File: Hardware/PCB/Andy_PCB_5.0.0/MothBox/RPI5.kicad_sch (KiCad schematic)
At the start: 4 parts, among them U16 Female Inv Socket Pi 2.54-2*20, U18 RASPBERRY_PI_4B_4GB, U4 RASPBERRY_PI_4B_4GB, U5 RASPBERRY_PI_5

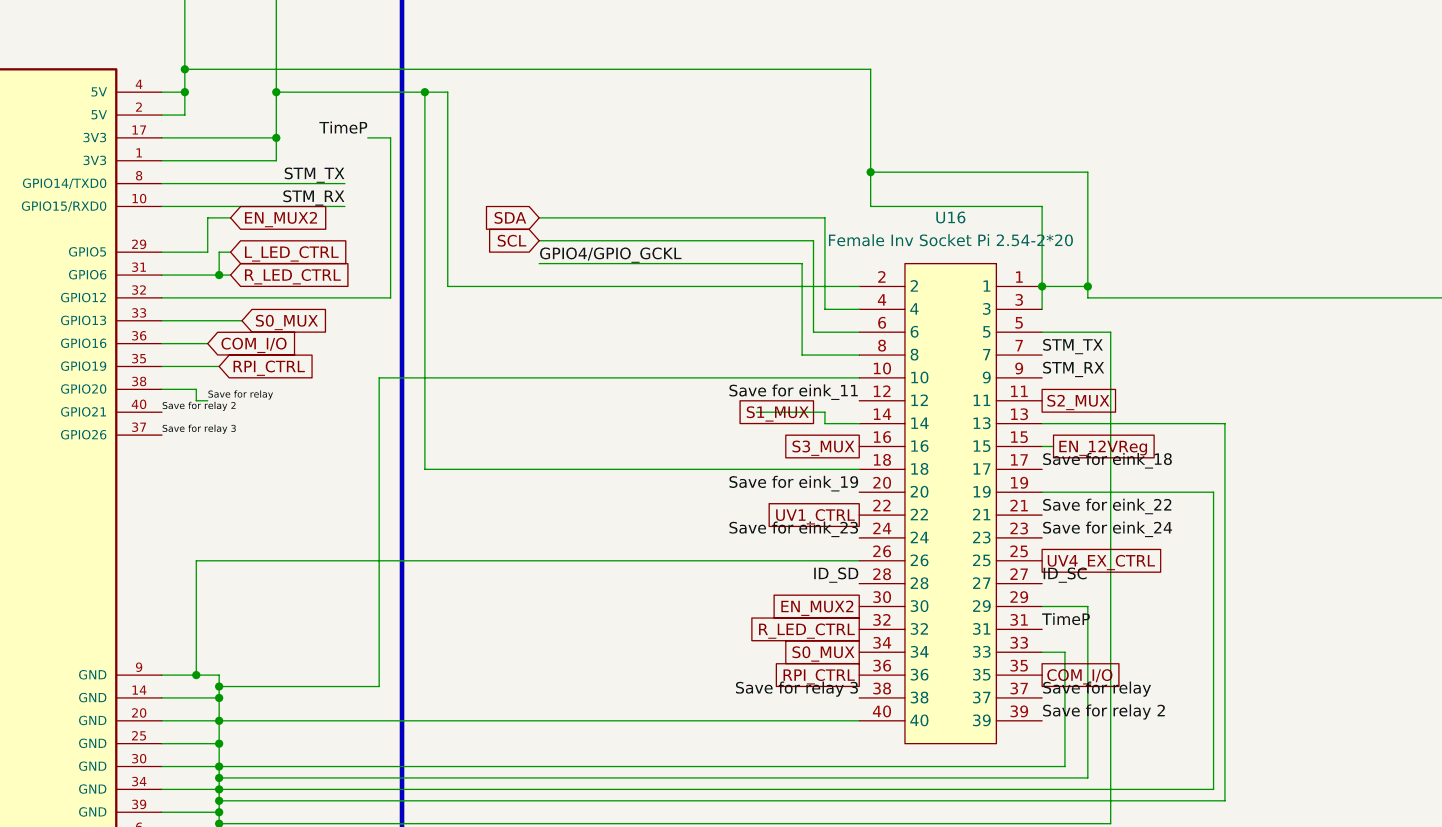
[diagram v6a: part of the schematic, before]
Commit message: added GPS 2 kinds
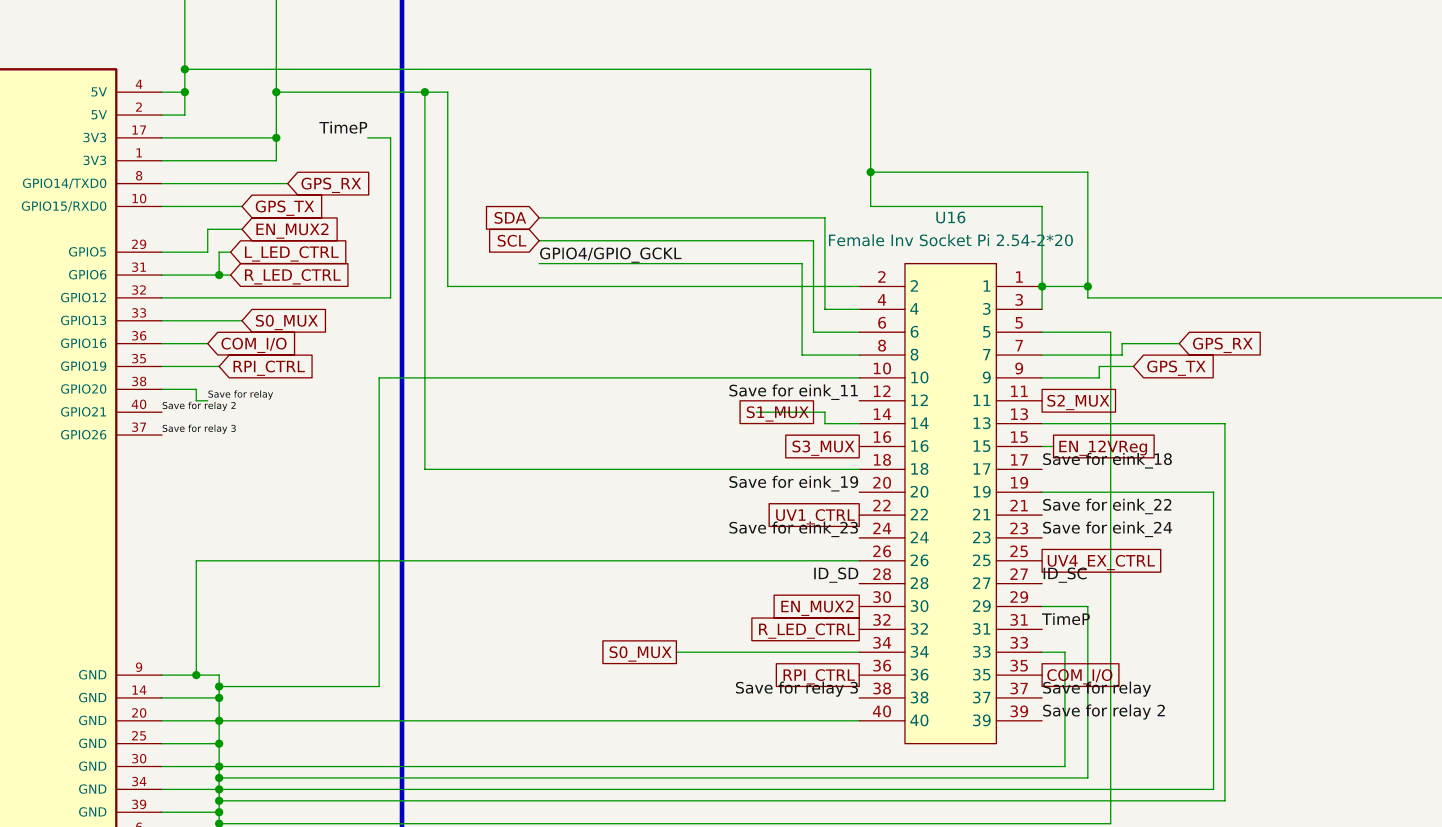
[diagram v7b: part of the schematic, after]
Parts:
- U5: footprint Connector_PinHeader_2.54mm:PinHeader_2x20_P2.54mm_Vertical -> AQLibrary:EPAPER_PinHeader_2x20_P2.54mm_Vertical
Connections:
- net STM_RX renamed GPS_TX
- net STM_TX renamed GPS_RX
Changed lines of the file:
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@@
+	(wire
+		(pts
+			(xy 153.67 102.87) (xy 173.99 102.87)
+		)
+		(stroke
+			(width 0)
+			(type default)
+		)
+	)
 	(wire
 		(pts
@@
 	(wire
 		(pts
-			(xy 96.52 53.34) (xy 116.84 53.34)
+			(xy 96.52 53.34) (xy 105.41 53.34)
 		)
 		(stroke
@@
 	(wire
 		(pts
+			(xy 200.66 72.39) (xy 200.66 71.12)
+		)
+		(stroke
+			(width 0)
+			(type default)
+		)
+	)
+	(wire
+		(pts
 			(xy 194.31 53.34) (xy 175.26 53.34)
 		)
@@
 	(wire
 		(pts
+			(xy 194.31 72.39) (xy 200.66 72.39)
+		)
+		(stroke
+			(width 0)
+			(type default)
+		)
+	)
+	(wire
+		(pts
 			(xy 102.87 110.49) (xy 173.99 110.49)
 		)
@@
 	(wire
 		(pts
-			(xy 101.6 54.61) (xy 104.14 54.61)
+			(xy 101.6 55.88) (xy 105.41 55.88)
 		)
 		(stroke
@@
 	(wire
 		(pts
-			(xy 96.52 50.8) (xy 116.84 50.8)
+			(xy 96.52 50.8) (xy 110.49 50.8)
 		)
 		(stroke
@@
 	(wire
 		(pts
+			(xy 203.2 69.85) (xy 203.2 68.58)
+		)
+		(stroke
+			(width 0)
+			(type default)
+		)
+	)
+	(wire
+		(pts
 			(xy 96.52 66.04) (xy 105.41 66.04)
 		)
@@
 	(wire
 		(pts
+			(xy 203.2 68.58) (xy 209.55 68.58)
+		)
+		(stroke
+			(width 0)
+			(type default)
+		)
+	)
+	(wire
+		(pts
 			(xy 173.99 72.39) (xy 120.65 72.39)
 		)
@@
 	(wire
 		(pts
+			(xy 194.31 69.85) (xy 203.2 69.85)
+		)
+		(stroke
+			(width 0)
+			(type default)
+		)
+	)
+	(wire
+		(pts
 			(xy 102.87 119.38) (xy 102.87 120.65)
 		)
@@
 	(wire
 		(pts
+			(xy 200.66 71.12) (xy 204.47 71.12)
+		)
+		(stroke
+			(width 0)
+			(type default)
+		)
+	)
+	(wire
+		(pts
 			(xy 170.18 64.77) (xy 170.18 54.61)
 		)
@@
 	(wire
 		(pts
-			(xy 101.6 54.61) (xy 101.6 58.42)
+			(xy 101.6 55.88) (xy 101.6 58.42)
 		)
 		(stroke
@@
 		)
 	)
-	(label "STM_TX"
-		(at 116.84 50.8 180)
-		(effects
-			(font
-				(size 1.27 1.27)
-			)
-			(justify right bottom)
-		)
-	)
 	(label "ID_SC"
 		(at 45.72 93.98 180)
@@
 		)
 	)
-	(label "STM_RX"
-		(at 194.31 72.39 0)
-		(effects
-			(font
-				(size 1.27 1.27)
-			)
-			(justify left bottom)
-		)
-	)
-	(label "STM_TX"
-		(at 194.31 69.85 0)
-		(effects
-			(font
-				(size 1.27 1.27)
-			)
-			(justify left bottom)
-		)
-	)
 	(label "Save for eink_23"
 		(at 45.72 81.28 180)
@@
 			(font
 				(size 0.762 0.762)
-			)
-			(justify right bottom)
-		)
-	)
-	(label "STM_RX"
-		(at 116.84 53.34 180)
-		(effects
-			(font
-				(size 1.27 1.27)
 			)
 			(justify right bottom)
@@
 	(global_label "S0_MUX"
 		(shape passive)
-		(at 173.99 102.87 180)
+		(at 153.67 102.87 180)
 		(effects
 			(font
@@
 		)
 		(property "Intersheetrefs" "${INTERSHEET_REFS}"
-			(at 173.99 102.87 0)
+			(at 153.67 102.87 0)
 			(effects
 				(font
@@
 		)
 	)
+	(global_label "GPS_RX"
+		(shape input)
+		(at 209.55 68.58 0)
+		(fields_autoplaced yes)
+		(effects
+			(font
+				(size 1.27 1.27)
+			)
+			(justify left)
+		)
+		(property "Intersheetrefs" "${INTERSHEET_REFS}"
+			(at 219.7318 68.58 0)
+			(effects
+				(font
+					(size 1.27 1.27)
+				)
+				(justify left)
+				(hide yes)
+			)
+		)
+	)
 	(global_label "SDA"
 		(shape input)
@@
 		)
 	)
+	(global_label "GPS_TX"
+		(shape input)
+		(at 204.47 71.12 0)
+		(fields_autoplaced yes)
+		(effects
+			(font
+				(size 1.27 1.27)
+			)
+			(justify left)
+		)
+		(property "Intersheetrefs" "${INTERSHEET_REFS}"
+			(at 214.3494 71.12 0)
+			(effects
+				(font
+					(size 1.27 1.27)
+				)
+				(justify left)
+				(hide yes)
+			)
+		)
+	)
 	(global_label "SCL"
 		(shape input)
@@
 		)
 	)
+	(global_label "GPS_RX"
+		(shape input)
+		(at 110.49 50.8 0)
+		(fields_autoplaced yes)
+		(effects
+			(font
+				(size 1.27 1.27)
+			)
+			(justify left)
+		)
+		(property "Intersheetrefs" "${INTERSHEET_REFS}"
+			(at 120.6718 50.8 0)
+			(effects
+				(font
+					(size 1.27 1.27)
+				)
+				(justify left)
+				(hide yes)
+			)
+		)
+	)
 	(global_label "R_LED_CTRL"
 		(shape passive)
@@
 	(global_label "EN_MUX2"
 		(shape input)
-		(at 104.14 54.61 0)
+		(at 105.41 55.88 0)
 		(fields_autoplaced yes)
 		(effects
@@
 		)
 		(property "Intersheetrefs" "${INTERSHEET_REFS}"
-			(at 115.7732 54.61 0)
+			(at 117.0432 55.88 0)
+			(effects
+				(font
+					(size 1.27 1.27)
+				)
+				(justify left)
+				(hide yes)
+			)
+		)
+	)
+	(global_label "GPS_TX"
+		(shape input)
+		(at 105.41 53.34 0)
+		(fields_autoplaced yes)
+		(effects
+			(font
+				(size 1.27 1.27)
+			)
+			(justify left)
+		)
+		(property "Intersheetrefs" "${INTERSHEET_REFS}"
+			(at 115.2894 53.34 0)
 			(effects
 				(font
@@
 			)
 		)
-		(property "Footprint" "Connector_PinHeader_2.54mm:PinHeader_2x20_P2.54mm_Vertical"
+		(property "Footprint" "AQLibrary:EPAPER_PinHeader_2x20_P2.54mm_Vertical"
 			(at 71.12 71.12 0)
 			(effects

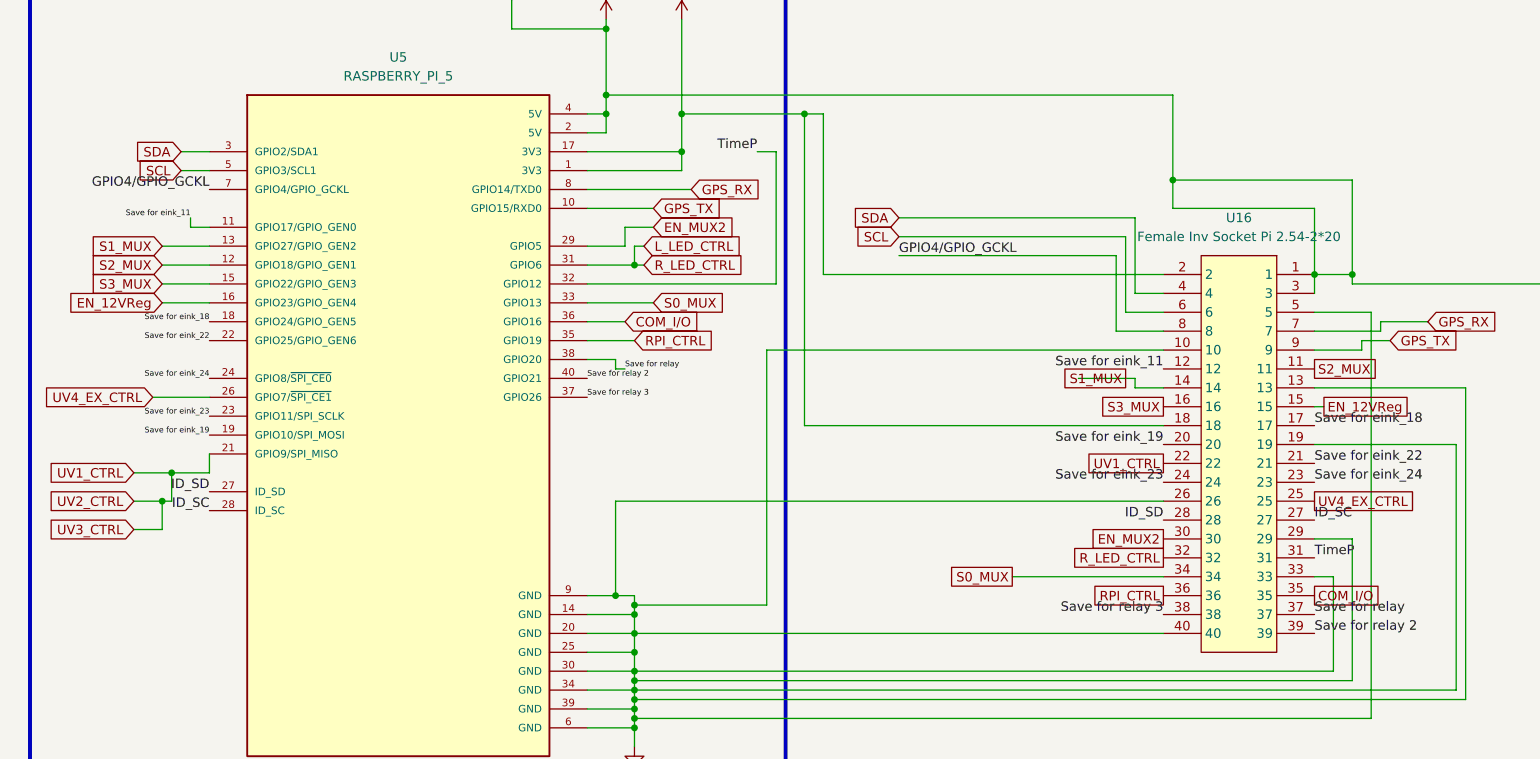
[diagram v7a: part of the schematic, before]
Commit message: Tweaked Mothbeam and added GPS footprints
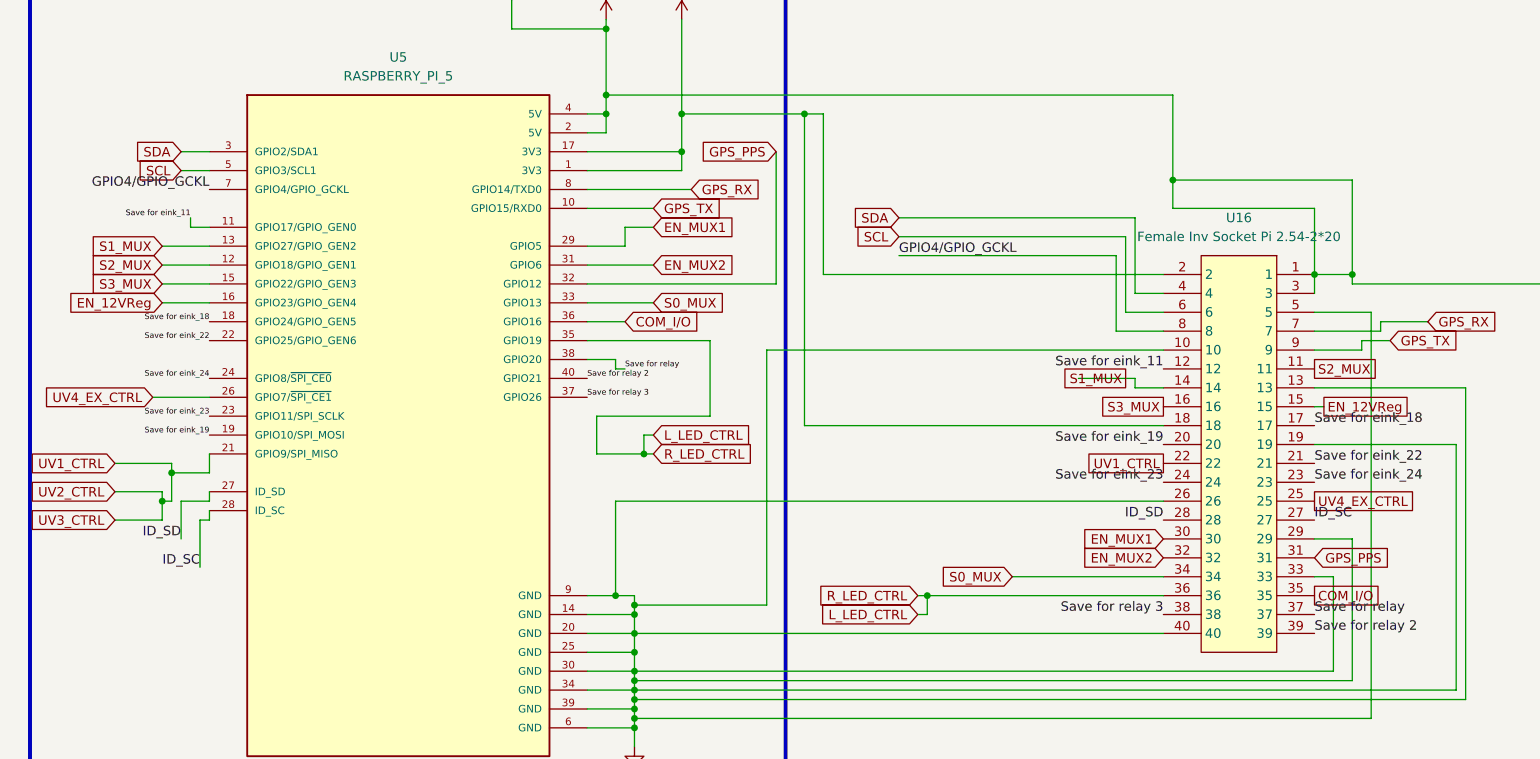
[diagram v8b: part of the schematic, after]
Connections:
- net RPI_CTRL is gone; now on net L_LED_CTRL: U16.36, U5.35 (GPIO19)
- net EN_MUX2: now also U16.32, U5.31 (GPIO6); no longer U16.30, U5.29 (GPIO5)
- net L_LED_CTRL: no longer U16.32, U5.31 (GPIO6)
- net TimeP renamed GPS_PPS
- new net EN_MUX1: U16.30, U5.29 (GPIO5)
